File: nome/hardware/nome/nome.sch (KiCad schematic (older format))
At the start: 4 parts

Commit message: Wire in more of the DAC. Decoupling caps
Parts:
- removed S?: PEC11R, symbol PEC11R
- removed SW?: SW_DIP_x01, symbol SW_DIP_x01
- added C? (x4): 100nF, symbol C
- added C?: 4.7uF, symbol C
- added C? (x6): 1uF, symbol C
- added C? (x6): 0.1uF, symbol C
- added C? (x2): 10uF, symbol C
- added C? (x2): 150pF, symbol C
- added J?: Audio-Jack-3_2Switches, symbol Audio-Jack-3_2Switches
- added LS? (x2): Speaker, symbol Speaker
- added SW?: SW_SPST, symbol SW_SPST
- added SW?: Rotary_Encoder_Switch, symbol Rotary_Encoder_Switch
- added U?: CS43L22, symbol CS43L22
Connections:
- net labels added: DAC_CK, DAC_MCK, DAC_RST, DAC_SCL, DAC_SD, DAC_SDA, DAC_WS, HP_A, HP_B, SPKR_A_NEG, SPKR_A_POS, SPKR_B_NEG, SPKR_B_POS
- wire segments 12 -> 127
- no-connect marks 0 -> 10
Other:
- moved on the sheet: BT?, U?

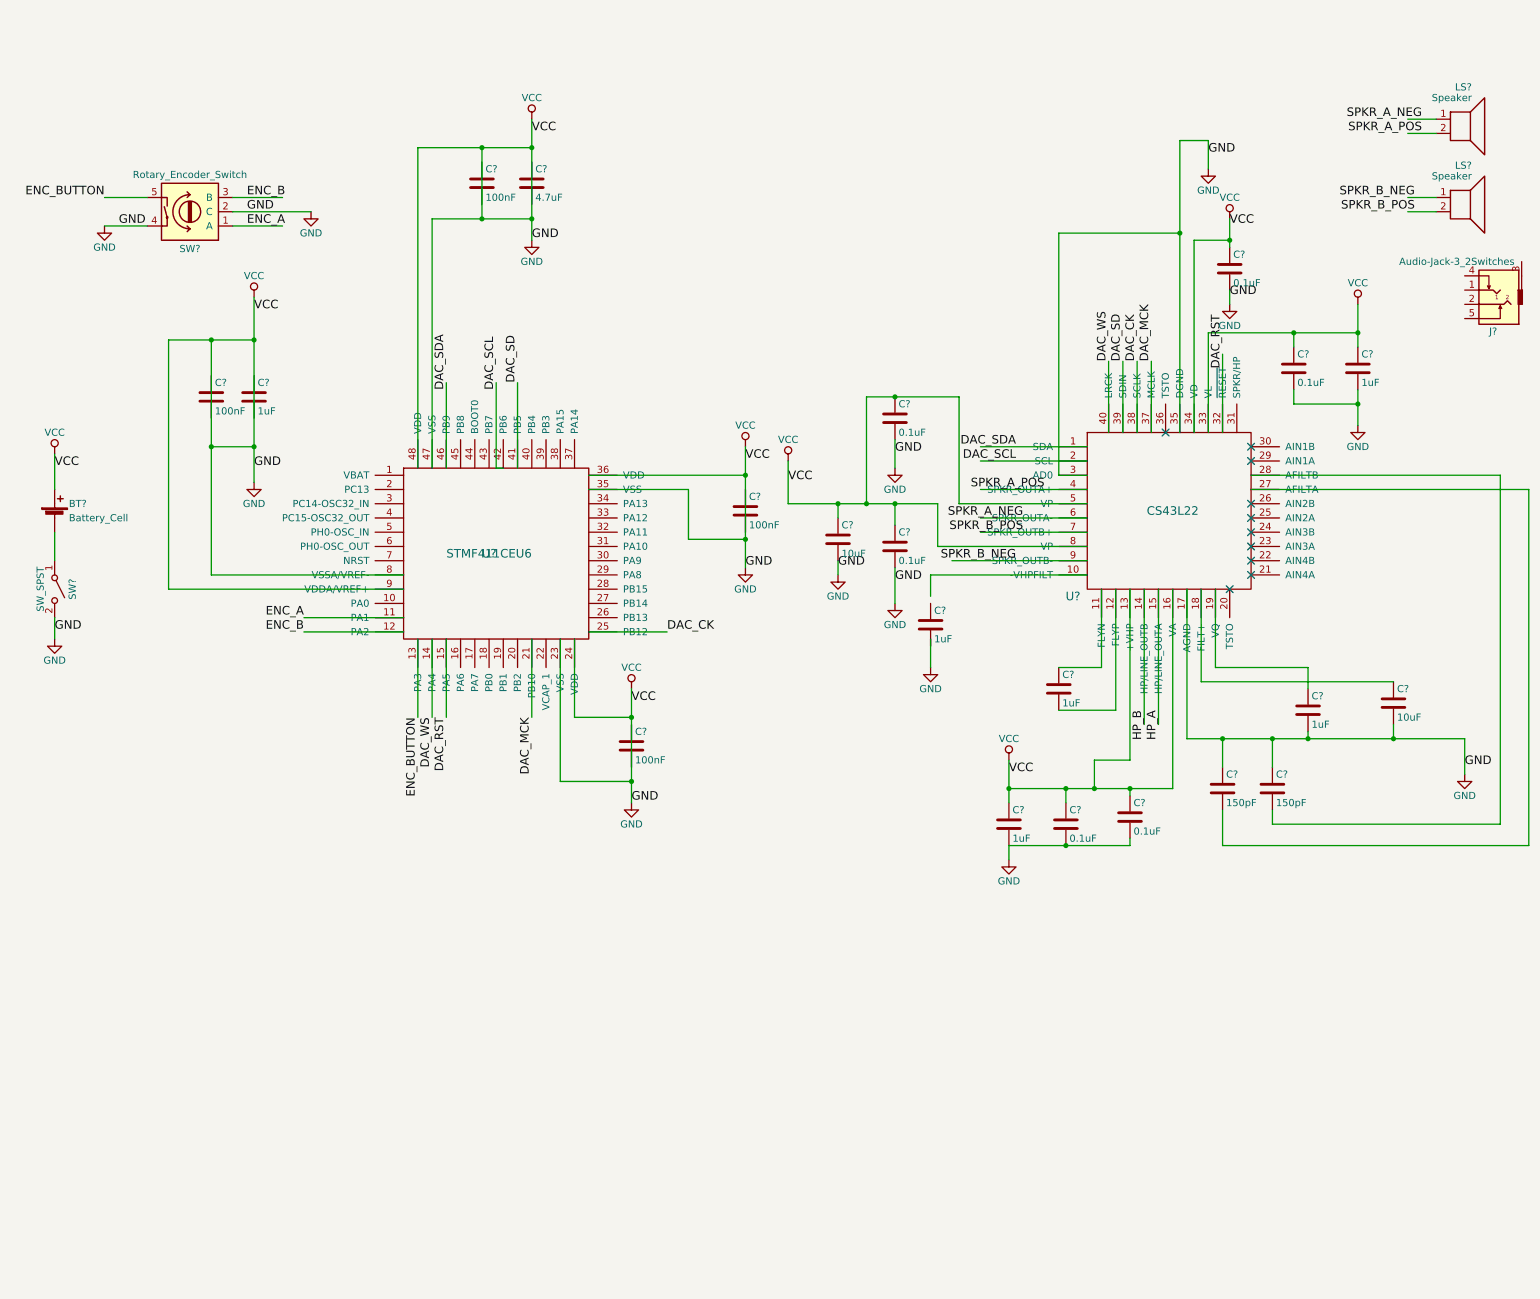
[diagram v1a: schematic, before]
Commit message: Add power regulators
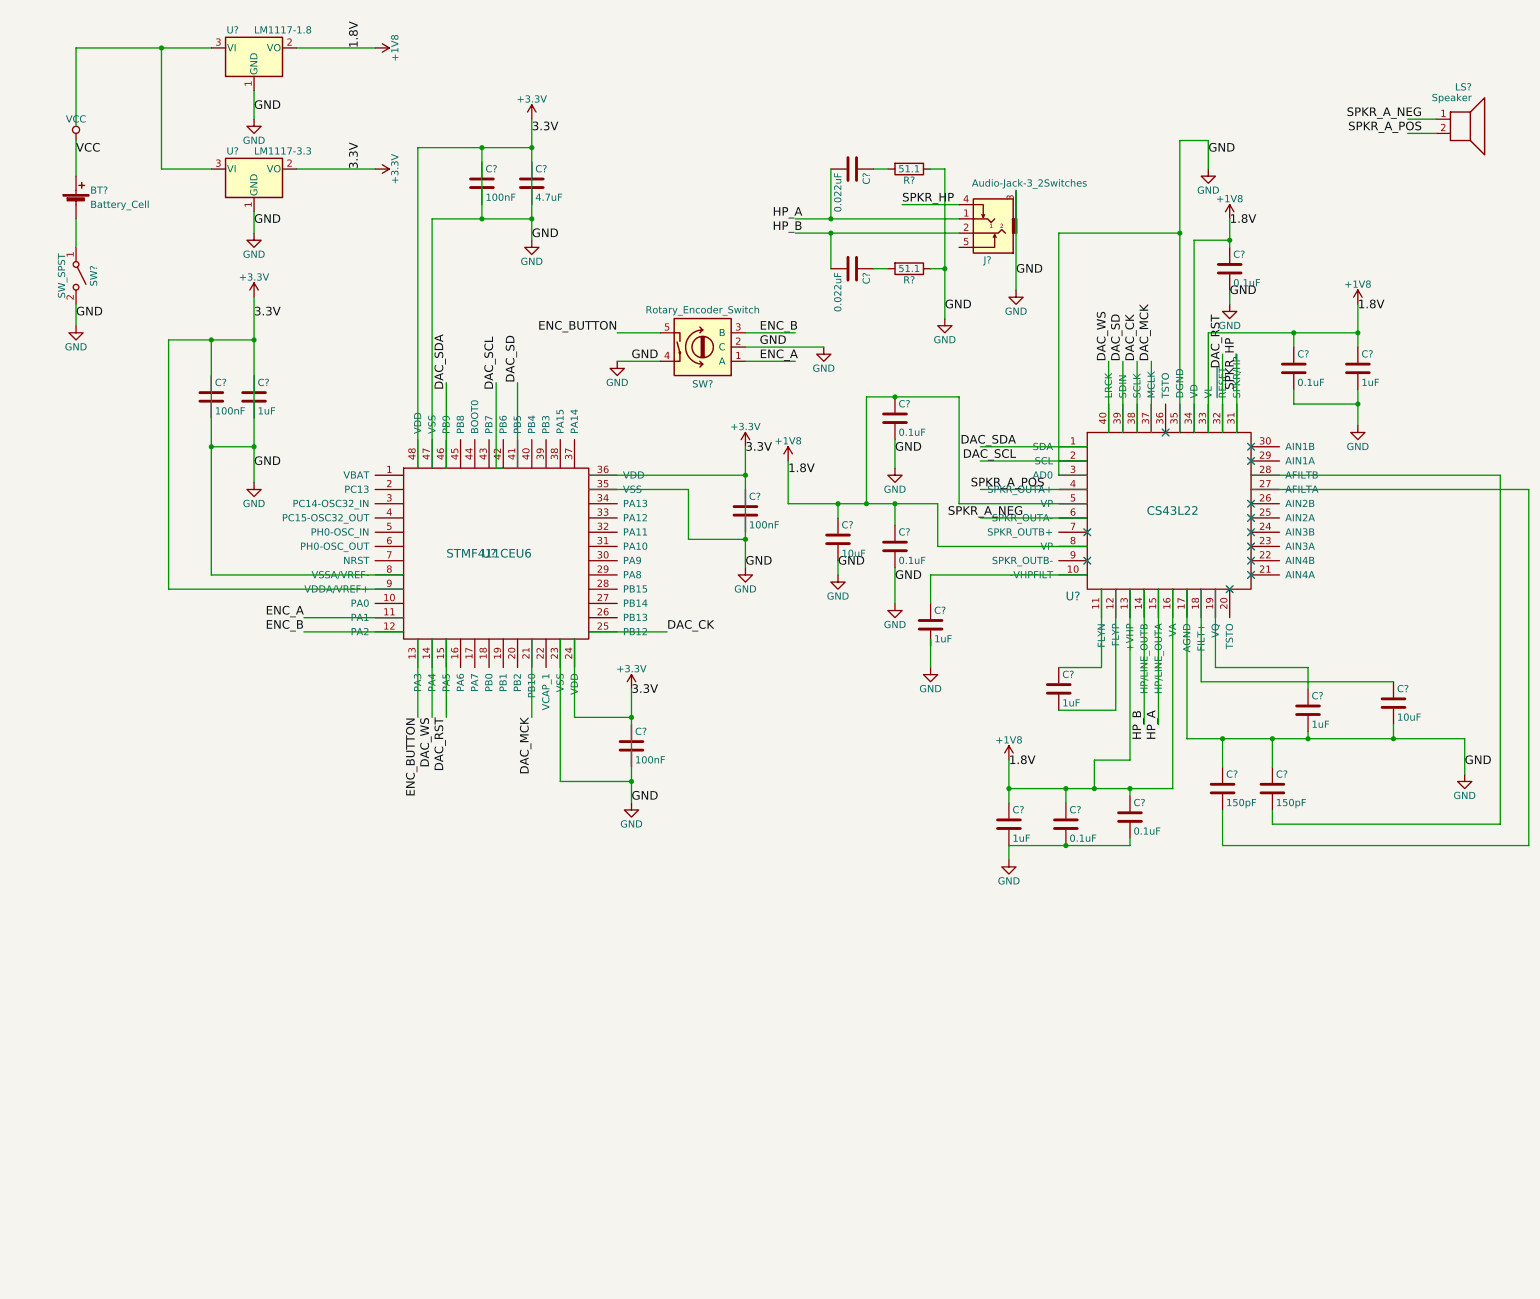
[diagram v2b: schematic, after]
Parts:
- removed LS?: Speaker, symbol Speaker
- added C? (x2): 0.022uF, symbol C
- added R? (x2): 51.1, symbol R
- added U?: LM1117-1.8, symbol LM1117-1.8
- added U?: LM1117-3.3, symbol LM1117-3.3
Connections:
- net labels added: +1V8, +3.3V, 1.8V, 3.3V, SPKR_HP
- net labels removed: SPKR_B_NEG, SPKR_B_POS
- wire segments 127 -> 143
- no-connect marks 10 -> 12
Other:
- moved on the sheet: BT?, J?, SW?

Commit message: Add 7segment schematic
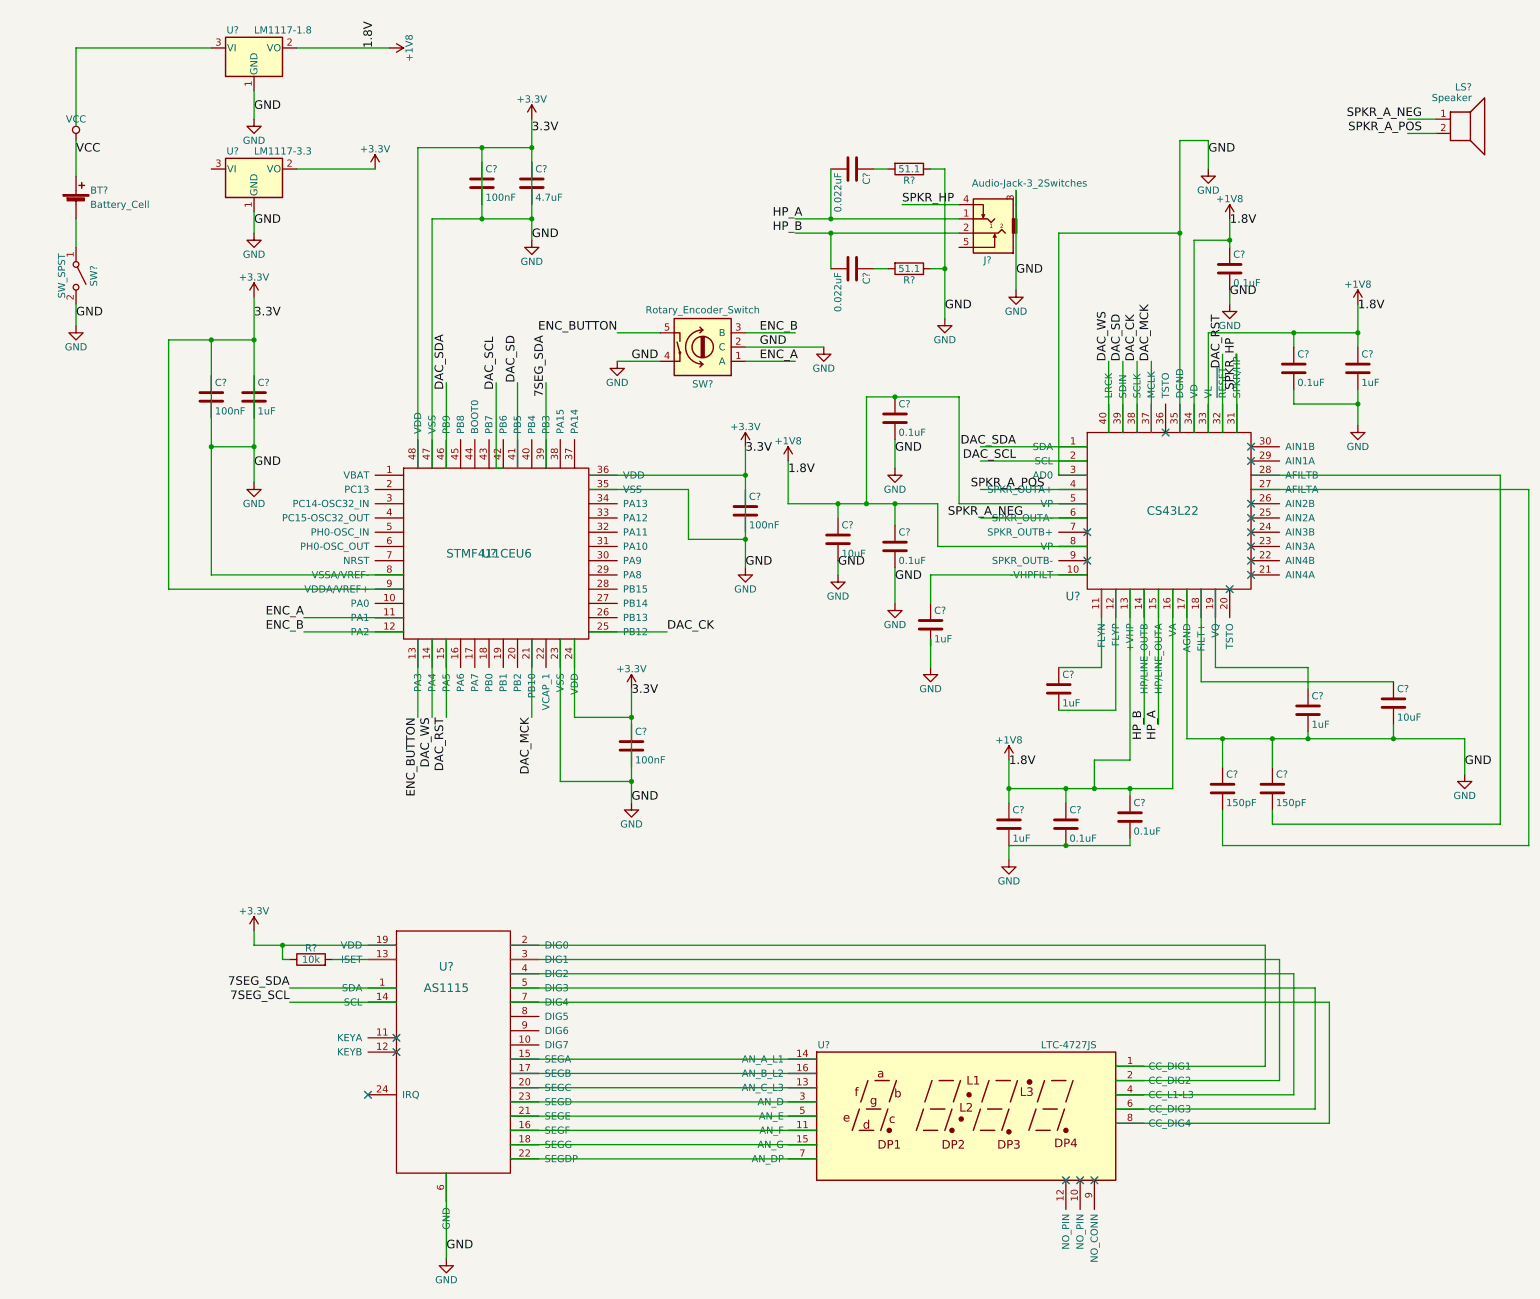
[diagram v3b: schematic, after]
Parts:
- added R?: 10k, symbol R
- added U?: AS1115, symbol AS1115
- added U?: LTC-4727JS, Displays_7-Segment:LTC-4727JS, symbol LTC-4727JS
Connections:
- net labels added: 7SEG_SCL, 7SEG_SDA
- wire segments 143 -> 173
- no-connect marks 12 -> 18

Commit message: Cap 7segment display, add status LEDs
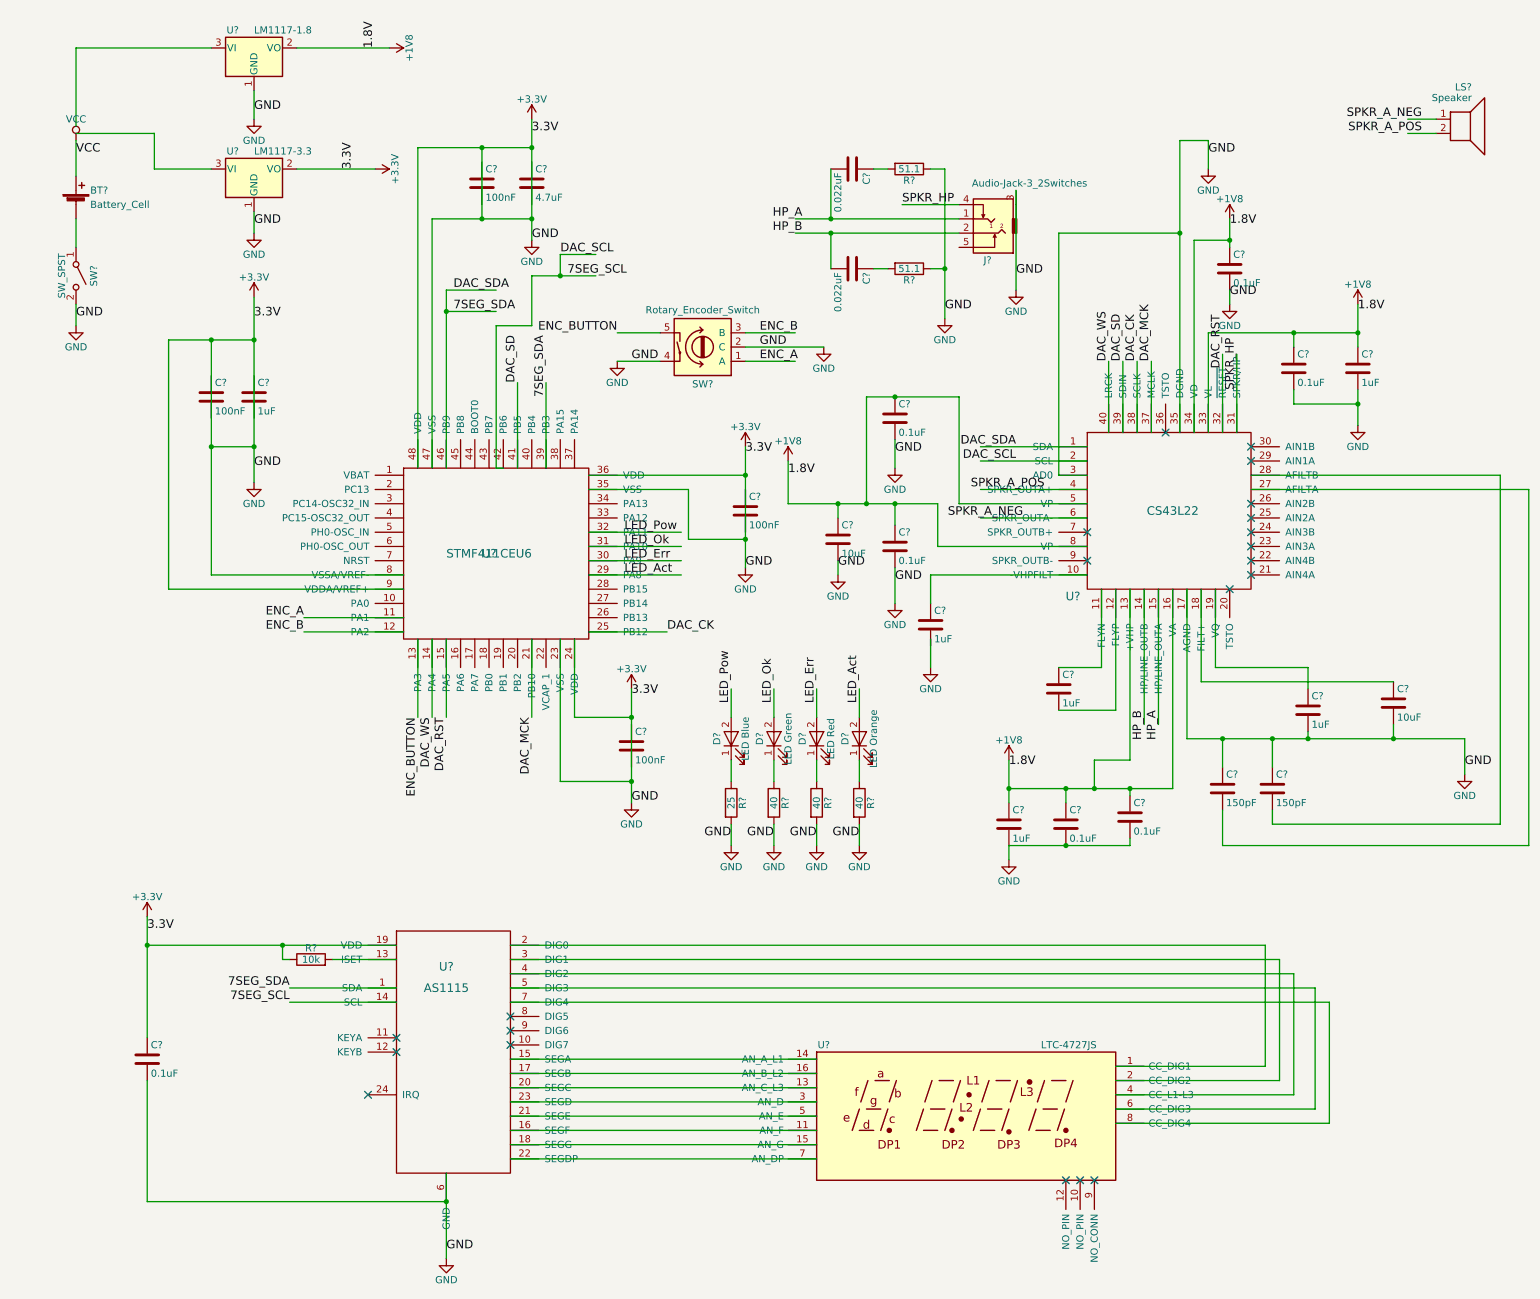
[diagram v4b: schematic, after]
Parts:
- removed U?: LTC-4727JS, Displays_7-Segment:LTC-4727JS, symbol LTC-4727JS
- added C?: 0.1uF, symbol C
- added D?: LED Orange, symbol LED
- added D?: LED Red, symbol LED
- added D?: LED Green, symbol LED
- added D?: LED Blue, symbol LED
- added R?: 25, symbol R
- added R? (x3): 40, symbol R
- added U?: LTC-4727JS, Displays_7-Segment:LTC-4727JS, symbol LTC-4727JS
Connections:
- net labels added: LED_Act, LED_Err, LED_Ok, LED_Pow
- wire segments 173 -> 201
- no-connect marks 18 -> 21

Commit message: Add JTAG header
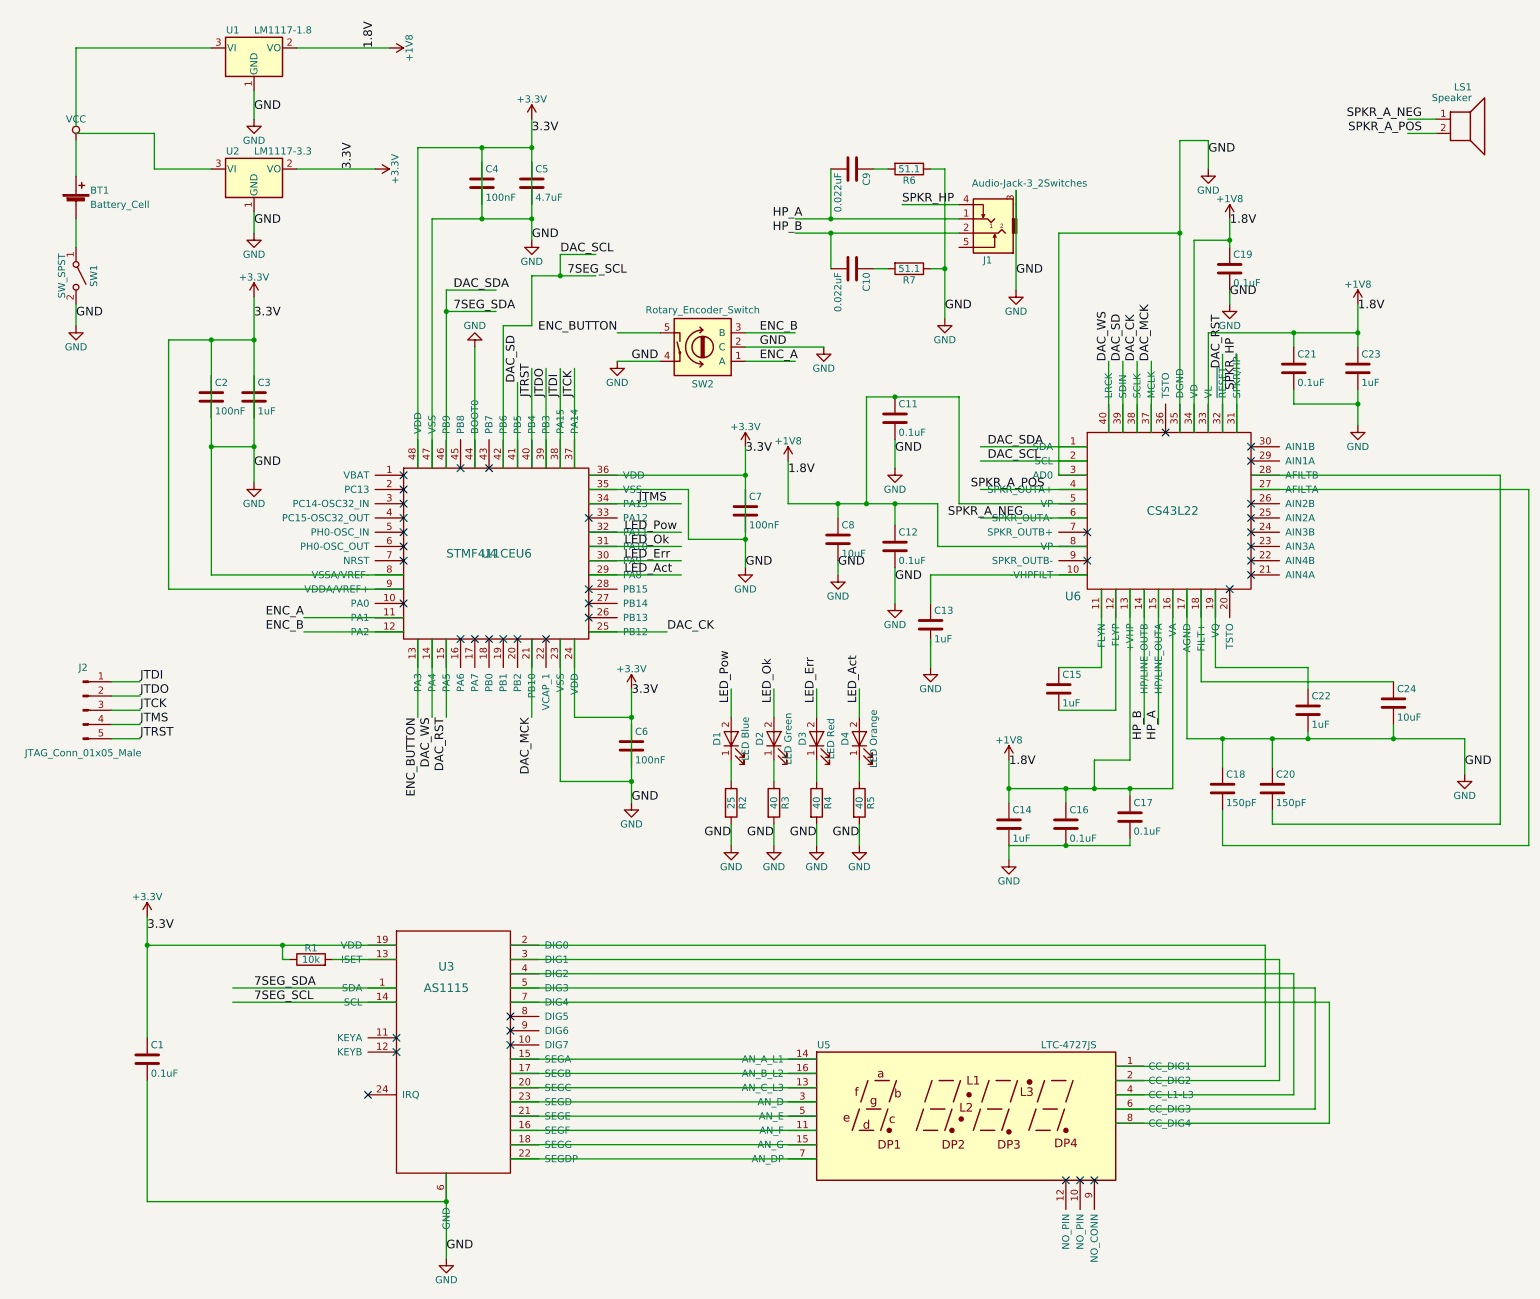
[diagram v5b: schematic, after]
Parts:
- added J2: JTAG_Conn_01x05_Male, symbol Conn_01x05_Male
- gave numbers to parts that had none: 46
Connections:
- net labels added: JTCK, JTDI, JTDO, JTMS, JTRST
- wire segments 201 -> 210
- no-connect marks 21 -> 41
